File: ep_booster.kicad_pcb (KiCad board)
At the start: 2 copper layers, 45.8 x 20.8 mm, 30 parts, among them J1 TB002-500-04BE, J2 Conn_01x04_Pin, Q1 MMBF5457, Q2 BC849C

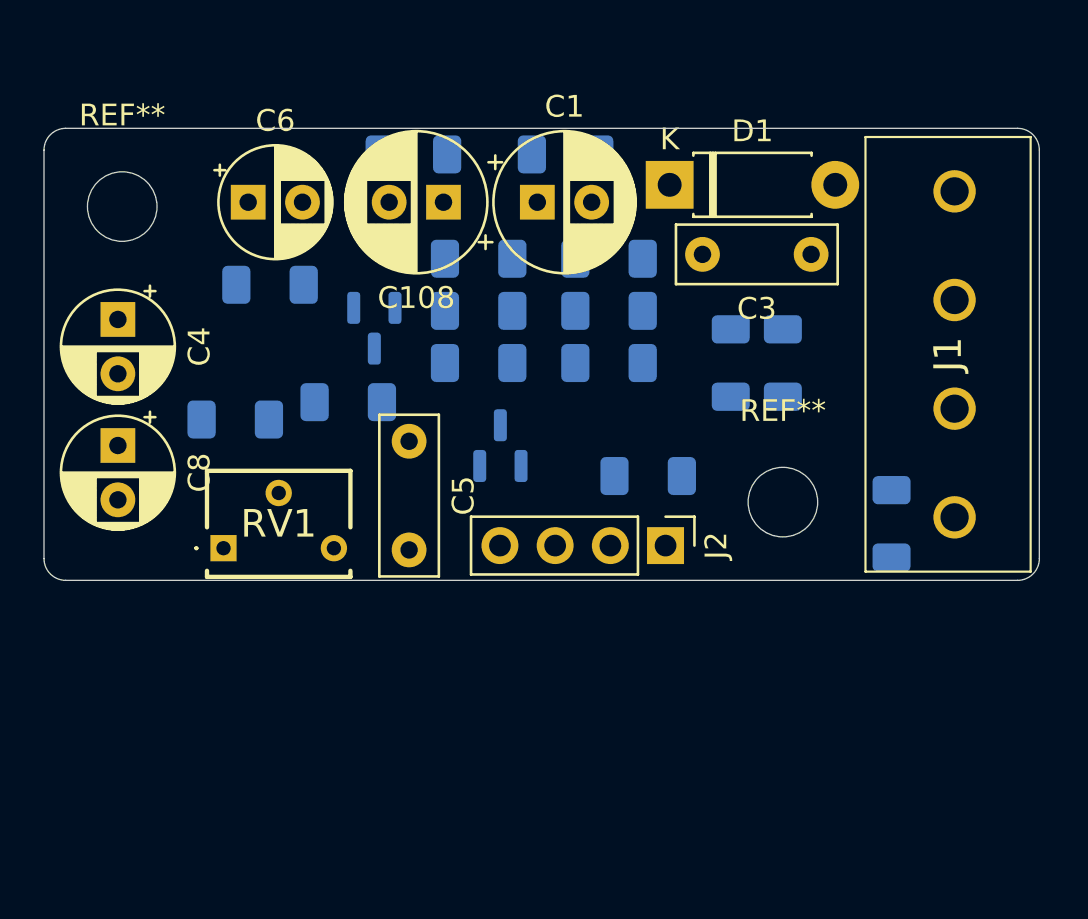
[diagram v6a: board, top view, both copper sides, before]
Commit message: tracing and copper field (GND) added
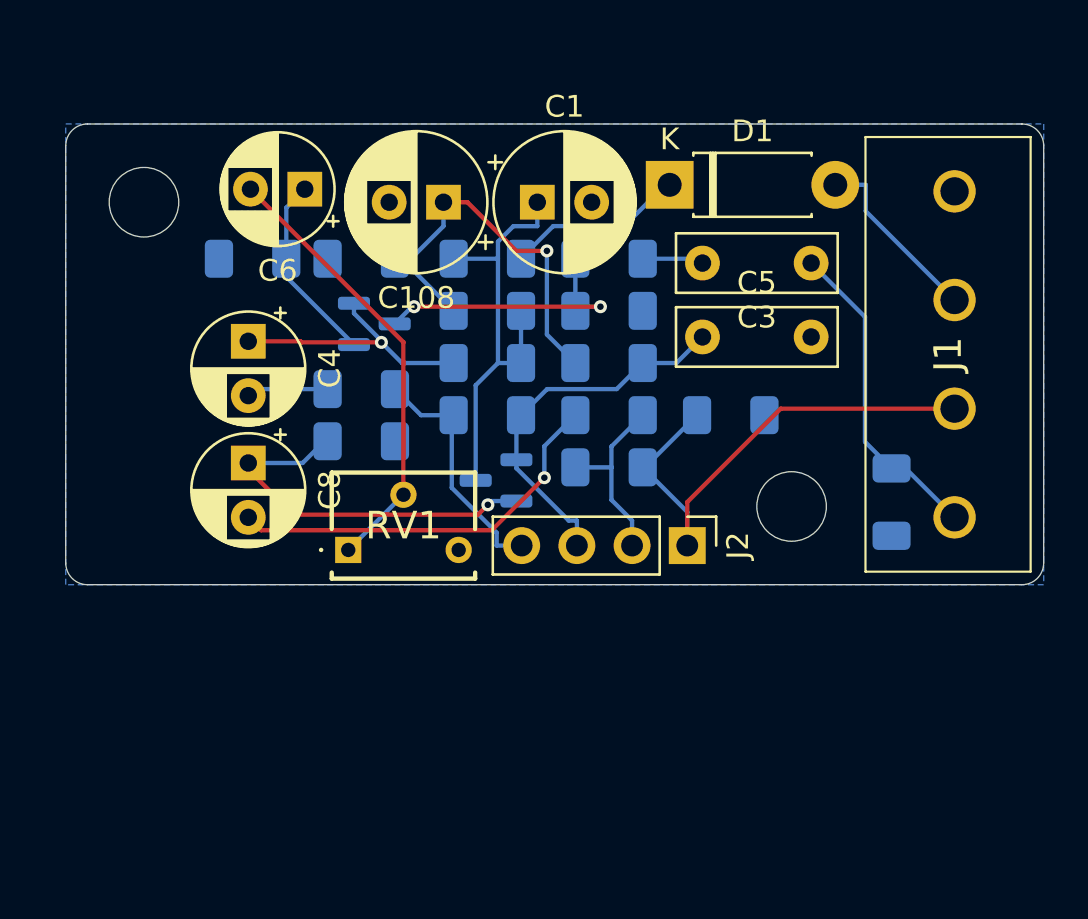
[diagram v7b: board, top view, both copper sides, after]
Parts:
- removed the REF** at (177.2, 79.0)
- removed the REF** at (207.6, 92.6)
- added REF**: MountingHole_3.2mm_M3, MountingHole:MountingHole_3.2mm_M3, F.Cu at (208.0, 92.8)
- added REF**: MountingHole_3.2mm_M3, MountingHole:MountingHole_3.2mm_M3, F.Cu at (178.2, 78.8)
- moved C5 14.3 mm to (203.9, 85.0), turned to 0 degrees
- moved R16 7.38 mm to (199.6, 91.0), turned to 0 degrees
- moved C4 6.08 mm to (183.0, 85.2)
- moved C8 6.05 mm to (183.0, 90.8)
- moved R1 6.00 mm to (194.0, 81.4)
- moved R11 5.89 mm to (188.2, 89.8)
- moved RV1 5.74 mm to (187.6, 94.8)
- moved R14 5.37 mm to (188.2, 81.4)
- moved R12 3.39 mm to (205.2, 88.6), turned to 180 degrees
- moved R9 3.33 mm to (199.6, 88.6)
- moved C6 2.67 mm to (185.6, 78.2), turned to 180 degrees
- moved R2 2.43 mm to (194.0, 86.2)
- moved R13 2.43 mm to (194.0, 83.8)
- moved R3 2.43 mm to (194.0, 88.6)
- moved Q2 1.61 mm to (194.4, 91.6), turned to 180 degrees
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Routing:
- net /OUT: track 0.00 -> 24.0 mm
- net Net-(C6-Pad2): track 0.00 -> 20.6 mm
- net VA: track 0.00 -> 20.1 mm
- net VB: track 0.00 -> 18.6 mm, vias 0 -> 1
- net Net-(C8-Pad2): track 0.00 -> 18.3 mm, vias 0 -> 1
- net Net-(Q2-E): track 0.00 -> 17.8 mm, vias 0 -> 1
- net /BRIGHT2: track 0.00 -> 17.3 mm
- net /IN: track 0.00 -> 14.8 mm
- net Net-(Q1-G): track 0.00 -> 13.3 mm, vias 0 -> 2
- net Net-(Q1-D): track 0.00 -> 12.2 mm, vias 0 -> 1
- net /BRIGHT1: track 0.00 -> 11.2 mm
- net Net-(Q1-S): track 0.00 -> 8.79 mm
- net Net-(J2-Pin_2): track 0.00 -> 8.65 mm
- net Net-(D1-A): track 0.00 -> 8.40 mm
- net Net-(D1-K): track 0.00 -> 8.26 mm
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- added copper zone on B.Cu, net GND
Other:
- board size 45.8 x 20.8 mm -> 45 x 21.2 mm
